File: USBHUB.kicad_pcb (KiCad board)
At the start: 6 copper layers, 89.8 x 89.8 mm, 251 parts, among them J1 USB_C_Receptacle, J2 R-RJ45R08P-C000, J3 Screw_Terminal_01x02, Q1 SI3421DV, Q2 SI3421DV, T1 G24P02S, U1 CYPD3177_24x, U10 USB_3_Type_A_Molex_484080003, U11 CYUSB3304-68LTXx, U12 TPS20xxC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

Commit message: fixing drcs
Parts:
- moved L2 0.60 mm to (116.4, 109.9)
- moved R3 0.16 mm to (82.7, 115.1)
- moved C46 0.10 mm to (99.6, 139.4)
- moved L1 0.08 mm to (133.5, 118.0)
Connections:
- U11 pad 30: HUB1_OVRCURR -> +3V3
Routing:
- net +1V2: track 130.8 -> 138.2 mm, vias 36 -> 38
- net +3V3: track 158.0 -> 165.0 mm, vias 52 -> 53
- net HUB1_OVRCURR: track 2.13 -> 0.00 mm, vias 1 -> 0
- net GND: track 259.3 -> 257.6 mm, vias 357 -> 437
- net +5V: track 241.9 -> 240.7 mm
- net /04 Hub Controller/DVDD12: track 52.3 -> 53.4 mm
- net HUB1_DS3_DP: track 85.1 -> 86.0 mm
- net HUB1_DS3_DN: track 85.1 -> 86.0 mm
- net HUB1_DS2_DN: track 59.8 -> 58.9 mm
- net HUB1_DS2_DP: track 59.8 -> 58.9 mm
- net USB_UFP_DN: track 58.3 -> 59.0 mm
- net USB_UFP_DP: track 58.5 -> 59.0 mm, vias 3 -> 2

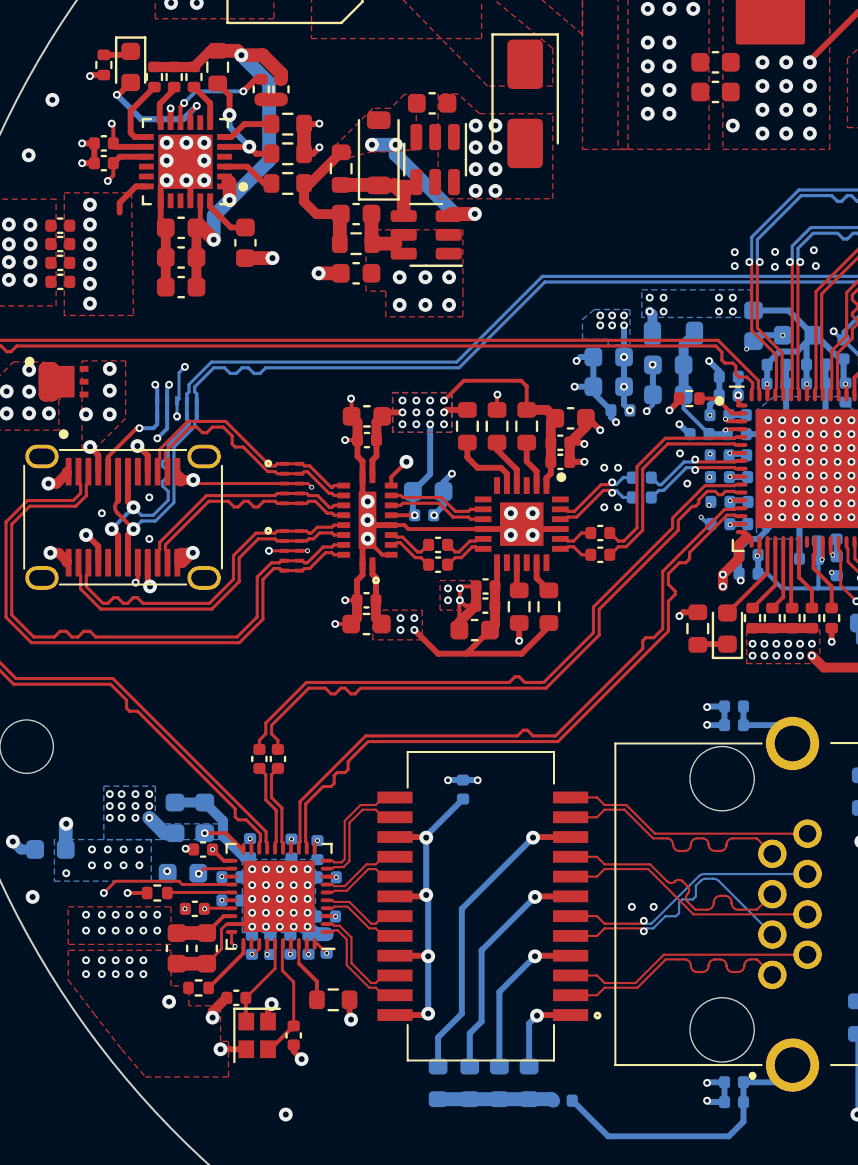
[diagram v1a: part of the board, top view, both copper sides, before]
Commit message: fix gnd plane splits
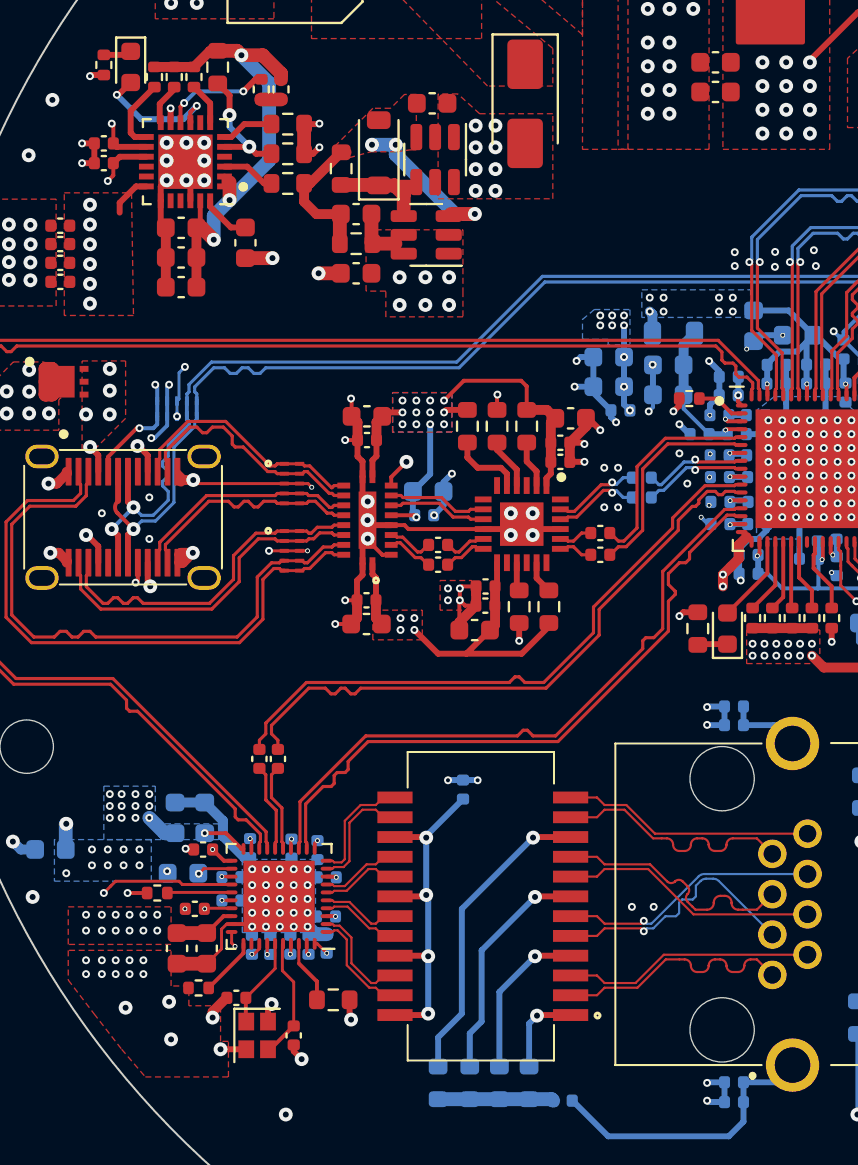
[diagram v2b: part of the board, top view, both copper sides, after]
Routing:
- net +3V3: track 165.0 -> 161.4 mm
- net GND: track 257.6 -> 257.5 mm, vias 437 -> 439
- net +5V: vias 71 -> 70
- added copper zone on In3.Cu, net +3V3
- added copper zone on In3.Cu, net +5V
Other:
- board text added: "cakeusb v1.0"

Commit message: finish bom list
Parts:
- C150: footprint Capacitor_SMD:C_0402_1005Metric -> Capacitor_SMD:C_1206_3216Metric
- C21, C23, C24: footprint Capacitor_SMD:C_0603_1608Metric -> Capacitor_SMD:C_0805_2012Metric
- D3: value Schottky -> SS54
- J2: value R-RJ45R08P-C000 -> RC01931; footprint CakeUSB:R-RJ45R08P-C000 -> CakeUSB:RC01931
- moved R48 14.2 mm to (125.7, 165.3)
- moved R49 10.1 mm to (125.7, 154.5)
- moved C82 3.85 mm to (130.9, 150.1), turned to -45 degrees
- moved C83 3.22 mm to (131.6, 149.4), turned to -45 degrees
- moved C122 3.01 mm to (142.8, 166.3)
- moved C123 3.01 mm to (135.4, 168.7)
- moved D10 3.01 mm to (137.0, 153.2)
- moved D11 3.01 mm to (146.9, 159.9)
- moved D17 3.01 mm to (132.8, 164.1)
- moved U9 3.01 mm to (137.0, 159.5)
- moved C124 3.01 mm to (139.7, 166.3)
- moved C125 3.01 mm to (141.2, 166.3)
- moved R40 3.01 mm to (143.6, 168.7)
- moved U14 3.01 mm to (141.0, 169.5)
- moved J2 2.73 mm to (119.3, 155.5), turned to 90 degrees
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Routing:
- net /05 Ethernet USB IC/LED_R+: track 61.7 -> 73.6 mm
- net GND: track 257.5 -> 264.2 mm, vias 439 -> 437
- net /05 Ethernet USB IC/LED_L+: track 50.8 -> 44.9 mm
- net HUB1_DS3_RXP: track 26.7 -> 30.2 mm
- net HUB1_DS3_RXN: track 26.7 -> 30.2 mm
- net /05 Ethernet USB IC/ETH2-: track 13.3 -> 9.81 mm
- net /05 Ethernet USB IC/ETH2+: track 13.3 -> 9.84 mm
- net /05 Ethernet USB IC/ETH4-: track 12.7 -> 9.35 mm
- net /05 Ethernet USB IC/ETH4+: track 12.6 -> 9.34 mm
- net /04 Hub Controller/HUB1_DS3_1_TXN: track 14.5 -> 17.8 mm
- net /04 Hub Controller/HUB1_DS3_1_TXP: track 14.5 -> 17.8 mm
- net /05 Ethernet USB IC/ETH3+: track 13.1 -> 10.1 mm
- net /05 Ethernet USB IC/ETH3-: track 13.0 -> 10.1 mm
- net HUB1_DS3_DP: track 86.0 -> 88.5 mm
- net HUB1_DS3_DN: track 86.0 -> 88.5 mm
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
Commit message: fix bom
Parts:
- added R50: 10k, Resistor_SMD:R_0402_1005Metric, F.Cu at (113.5, 141.2)
- added R51: 10k, Resistor_SMD:R_0402_1005Metric, B.Cu at (112.2, 140.9)
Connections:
- U11 pad 17: +5V -> Net-(U11-VBUS_US)
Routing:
- net Net-(U11-VBUS_US): track 0.00 -> 3.45 mm, vias 0 -> 1
- net GND: track 264.2 -> 266.4 mm, vias 437 -> 438
- net Net-(U15A-RSET): track 4.65 -> 3.77 mm
- net +5V: track 243.1 -> 242.3 mm, vias 70 -> 69
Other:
- board text added: "20V"
- board text added: "5V GOOD"
- board text added: "GND"
- board text added: "PD FAULT"
- board text added: "SUSPEND"
